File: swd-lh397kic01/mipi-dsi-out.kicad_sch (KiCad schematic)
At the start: 7 parts, among them J2 DF40C-24DS-0.4V_51_, SW1 SMD-BUTTON_4P-5.2X5.2X1.5MM-S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

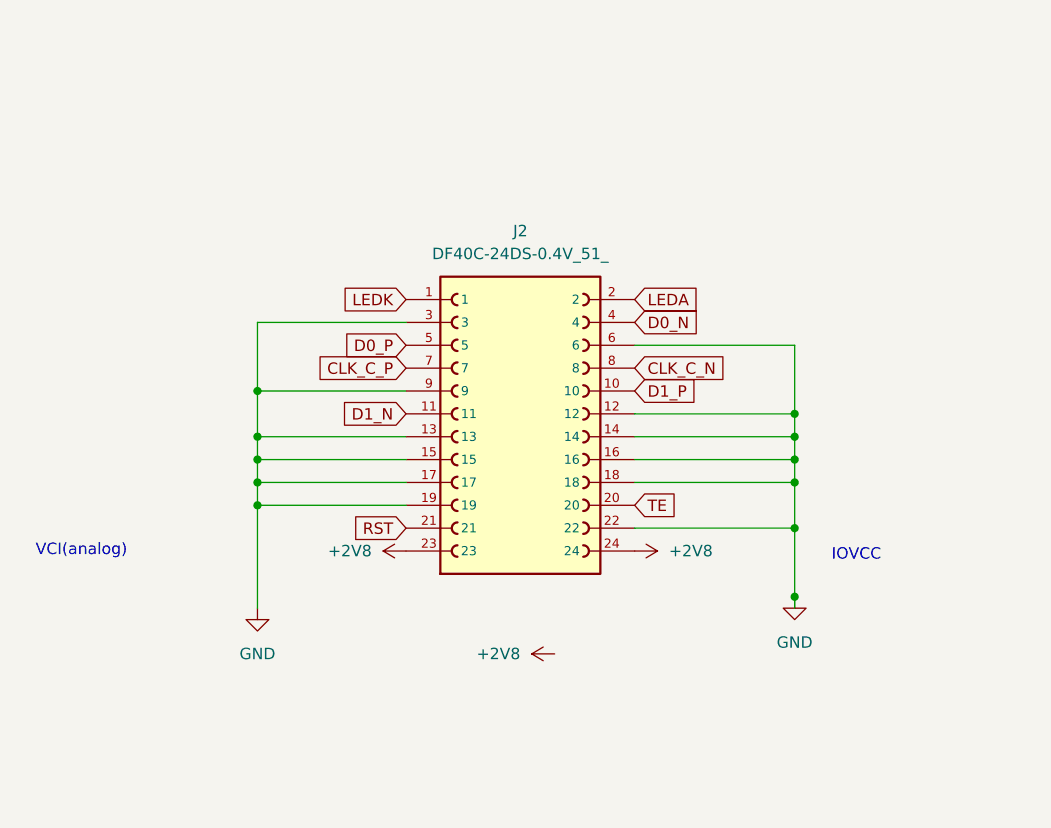
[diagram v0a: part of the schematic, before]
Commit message: Add LCSC labels that were missing for swd lh397kic01
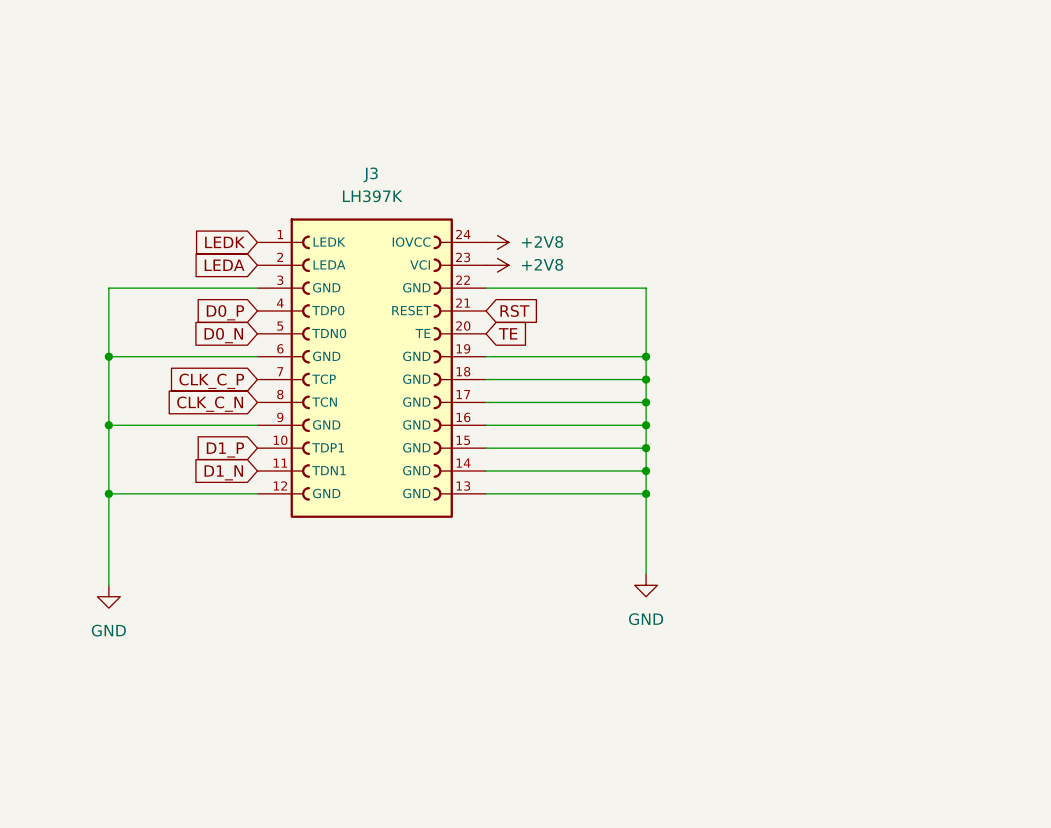
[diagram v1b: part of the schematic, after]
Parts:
- removed J2: DF40C-24DS-0.4V_51_, custom:HIROSE_DF40C-24DS-0.4V_51_, symbol DF40C-24DS-0.4V_51_:DF40C-24DS-0.4V_51_
- added J3: LH397K, custom:LH397K-IC01, symbol LH397K-IC01:LH397K-IC01
- C4: LCSC C5189821 -> C386149
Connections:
- net +2V8: now also J3.23 (VCI), J3.24 (IOVCC)
- net CLK_C_N: now also J3.8 (TCN)
- net CLK_C_P: now also J3.7 (TCP)
- net D0_N: now also J3.5 (TDN0)
- net D0_P: now also J3.4 (TDP0)
- net D1_N: now also J3.11 (TDN1)
- net D1_P: now also J3.10 (TDP1)
- net GND: now also J3.12 (GND), J3.13 (GND), J3.14 (GND), J3.15 (GND), J3.16 (GND), J3.17 (GND), J3.18 (GND), J3.19 (GND), J3.22 (GND), J3.3 (GND), J3.6 (GND), J3.9 (GND)
- net LEDA: now also J3.2 (LEDA)
- net LEDK: now also J3.1 (LEDK)
- net RST: now also J3.21 (RESET)
- net TE: now also J3.20 (TE)
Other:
- note removed: "IOVCC"
- note removed: "VCI(analog)"
